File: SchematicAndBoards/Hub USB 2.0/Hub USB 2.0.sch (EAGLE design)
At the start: 29 parts, among them IC1 STM32F10XCXT6, IC2 MCP1703CB, IC3 IC_USBLC6-2, Q1 KX-7T 16.0 MHz, X1 USB-A

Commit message: Update schematic and boards
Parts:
- IC1: device stm32F:STM32F10XCXT6 -> stm32:STM32F10XCXT6
- IC3: value IC_USBLC6-2 -> USBLC6
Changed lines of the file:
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@@
 <?xml version="1.0" encoding="utf-8"?>
 <!DOCTYPE eagle SYSTEM "eagle.dtd">
-<eagle version="7.7.0">
+<eagle version="8.2.1">
 <drawing>
 <settings>
@@
 <layer number="56" name="wert" color="7" fill="1" visible="no" active="no"/>
 <layer number="57" name="tCAD" color="7" fill="1" visible="no" active="no"/>
+<layer number="59" name="tCarbon" color="7" fill="1" visible="no" active="no"/>
+<layer number="60" name="bCarbon" color="7" fill="1" visible="no" active="no"/>
 <layer number="90" name="Modules" color="5" fill="1" visible="yes" active="yes"/>
 <layer number="91" name="Nets" color="2" fill="1" visible="yes" active="yes"/>
@@
 <layer number="127" name="_tValues" color="7" fill="1" visible="no" active="yes"/>
 <layer number="128" name="_bValues" color="7" fill="1" visible="no" active="yes"/>
+<layer number="129" name="Mask" color="7" fill="1" visible="yes" active="yes"/>
 <layer number="131" name="tAdjust" color="7" fill="1" visible="no" active="yes"/>
 <layer number="132" name="bAdjust" color="7" fill="1" visible="no" active="yes"/>
@@
 <layer number="223" name="223bmp" color="24" fill="1" visible="no" active="no"/>
 <layer number="224" name="224bmp" color="25" fill="1" visible="no" active="no"/>
+<layer number="225" name="225bmp" color="7" fill="1" visible="yes" active="yes"/>
+<layer number="226" name="226bmp" color="7" fill="1" visible="yes" active="yes"/>
+<layer number="227" name="227bmp" color="7" fill="1" visible="yes" active="yes"/>
+<layer number="228" name="228bmp" color="7" fill="1" visible="yes" active="yes"/>
+<layer number="229" name="229bmp" color="7" fill="1" visible="yes" active="yes"/>
+<layer number="230" name="230bmp" color="7" fill="1" visible="yes" active="yes"/>
 <layer number="231" name="Eagle3D_PG1" color="7" fill="1" visible="no" active="no"/>
 <layer number="232" name="Eagle3D_PG2" color="7" fill="1" visible="no" active="no"/>
@@
 <layer number="251" name="SMDround" color="7" fill="1" visible="no" active="no"/>
 <layer number="254" name="cooling" color="7" fill="1" visible="no" active="yes"/>
+<layer number="255" name="routoute" color="7" fill="1" visible="yes" active="yes"/>
 </layers>
 <schematic xreflabel="%F%N/%S.%C%R" xrefpart="/%S.%C%R">
@@
 <parts>
 <part name="X1" library="adafruit" deviceset="USB-A" device=""/>
-<part name="IC1" library="stm32F" deviceset="STM32F10XCXT6" device=""/>
+<part name="IC1" library="stm32" deviceset="STM32F10XCXT6" device=""/>
 <part name="Q1" library="Eagle-JeeLabs" deviceset="CRYSTAL" device="3.2X2.5" value="KX-7T 16.0 MHz"/>
 <part name="R1" library="resistor" deviceset="R-EU_" device="R0805" value="22"/>
@@
 <part name="C11" library="resistor" deviceset="C-EU" device="C0805" value="0.01uF"/>
 <part name="C12" library="resistor" deviceset="C-EU" device="C0805" value="0.01uF"/>
-<part name="IC3" library="dp_devices" deviceset="IC_USBLC6-2" device=""/>
+<part name="IC3" library="dp_devices" deviceset="IC_USBLC6-2" device="" value="USBLC6"/>
 <part name="Q2" library="semicon-smd-ipc" deviceset="PNP-TRANSISTOR_" device="SOT23"/>
 <part name="U$2" library="RemoteSwitchComponents" deviceset="AS07-M1101S" device=""/>

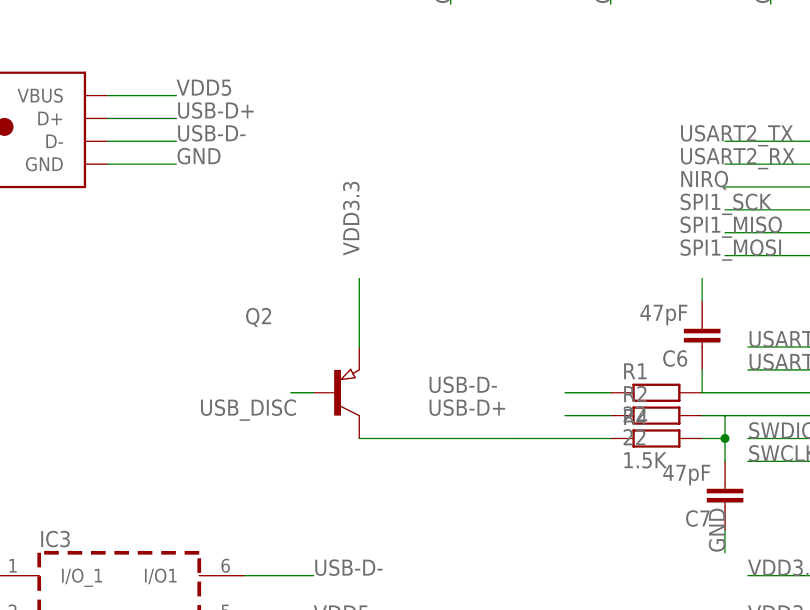
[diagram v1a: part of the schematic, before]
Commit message: Update Hub USB 2.0 schematic
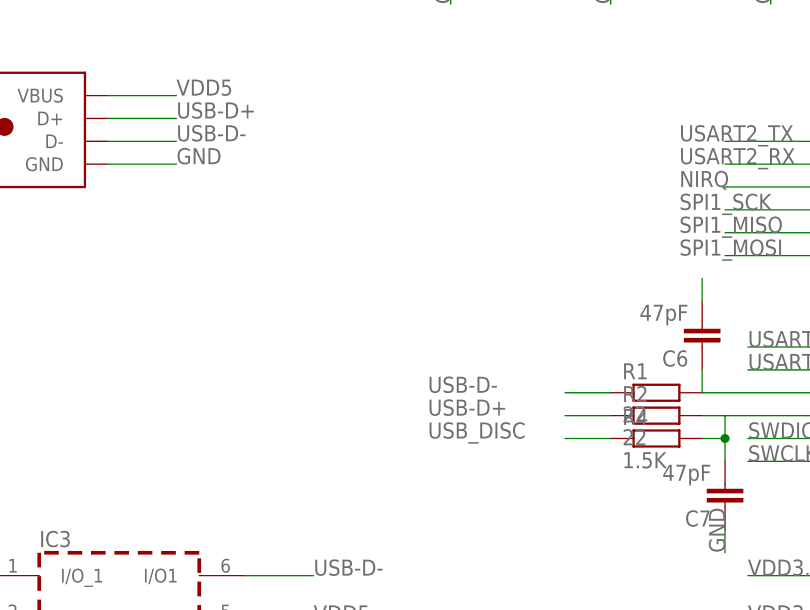
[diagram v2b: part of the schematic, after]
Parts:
- removed Q2: (no value), semicon-smd-ipc:PNP-TRANSISTOR_SOT23
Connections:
- removed net N$8: Q2.C, R4.1
- net USB_DISC: now also R4.1; no longer Q2.B
- net VDD3.3: no longer Q2.E
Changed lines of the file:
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@@
 <?xml version="1.0" encoding="utf-8"?>
 <!DOCTYPE eagle SYSTEM "eagle.dtd">
-<eagle version="8.2.1">
+<eagle version="7.7.0">
 <drawing>
 <settings>
@@
 <part name="C12" library="resistor" deviceset="C-EU" device="C0805" value="0.01uF"/>
 <part name="IC3" library="dp_devices" deviceset="IC_USBLC6-2" device="" value="USBLC6"/>
-<part name="Q2" library="semicon-smd-ipc" deviceset="PNP-TRANSISTOR_" device="SOT23"/>
 <part name="U$2" library="RemoteSwitchComponents" deviceset="AS07-M1101S" device=""/>
 </parts>
@@
 <instance part="C12" gate="G$1" x="114.3" y="109.22" rot="R180"/>
 <instance part="IC3" gate="G$1" x="2.54" y="22.86"/>
-<instance part="Q2" gate="G$1" x="17.78" y="55.88"/>
 <instance part="U$2" gate="G$1" x="182.88" y="-10.16"/>
 </instances>
@@
 </segment>
 <segment>
-<pinref part="Q2" gate="G$1" pin="E"/>
-<wire x1="20.32" y1="60.96" x2="20.32" y2="68.58" width="0.1524" layer="91"/>
-<label x="20.32" y="71.12" size="1.778" layer="95" rot="R90"/>
-</segment>
-<segment>
 <pinref part="U$2" gate="G$1" pin="VDD"/>
 <wire x1="170.18" y1="0" x2="157.48" y2="0" width="0.1524" layer="91"/>
@@
 </segment>
 </net>
-<net name="N$8" class="0">
-<segment>
-<pinref part="Q2" gate="G$1" pin="C"/>
-<wire x1="20.32" y1="50.8" x2="38.1" y2="50.8" width="0.1524" layer="91"/>
-</segment>
-<segment>
-<pinref part="R4" gate="G$1" pin="1"/>
-<wire x1="48.26" y1="50.8" x2="38.1" y2="50.8" width="0.1524" layer="91"/>
-</segment>
-</net>
 <net name="USB_DISC" class="0">
 <segment>
@@
 </segment>
 <segment>
-<pinref part="Q2" gate="G$1" pin="B"/>
-<wire x1="15.24" y1="55.88" x2="12.7" y2="55.88" width="0.1524" layer="91"/>
-<label x="2.54" y="53.34" size="1.778" layer="95"/>
-</segment>
-</net>
+<pinref part="R4" gate="G$1" pin="1"/>
+<wire x1="48.26" y1="50.8" x2="43.18" y2="50.8" width="0.1524" layer="91"/>
+<label x="27.94" y="50.8" size="1.778" layer="95"/>
+</segment>
+</net>

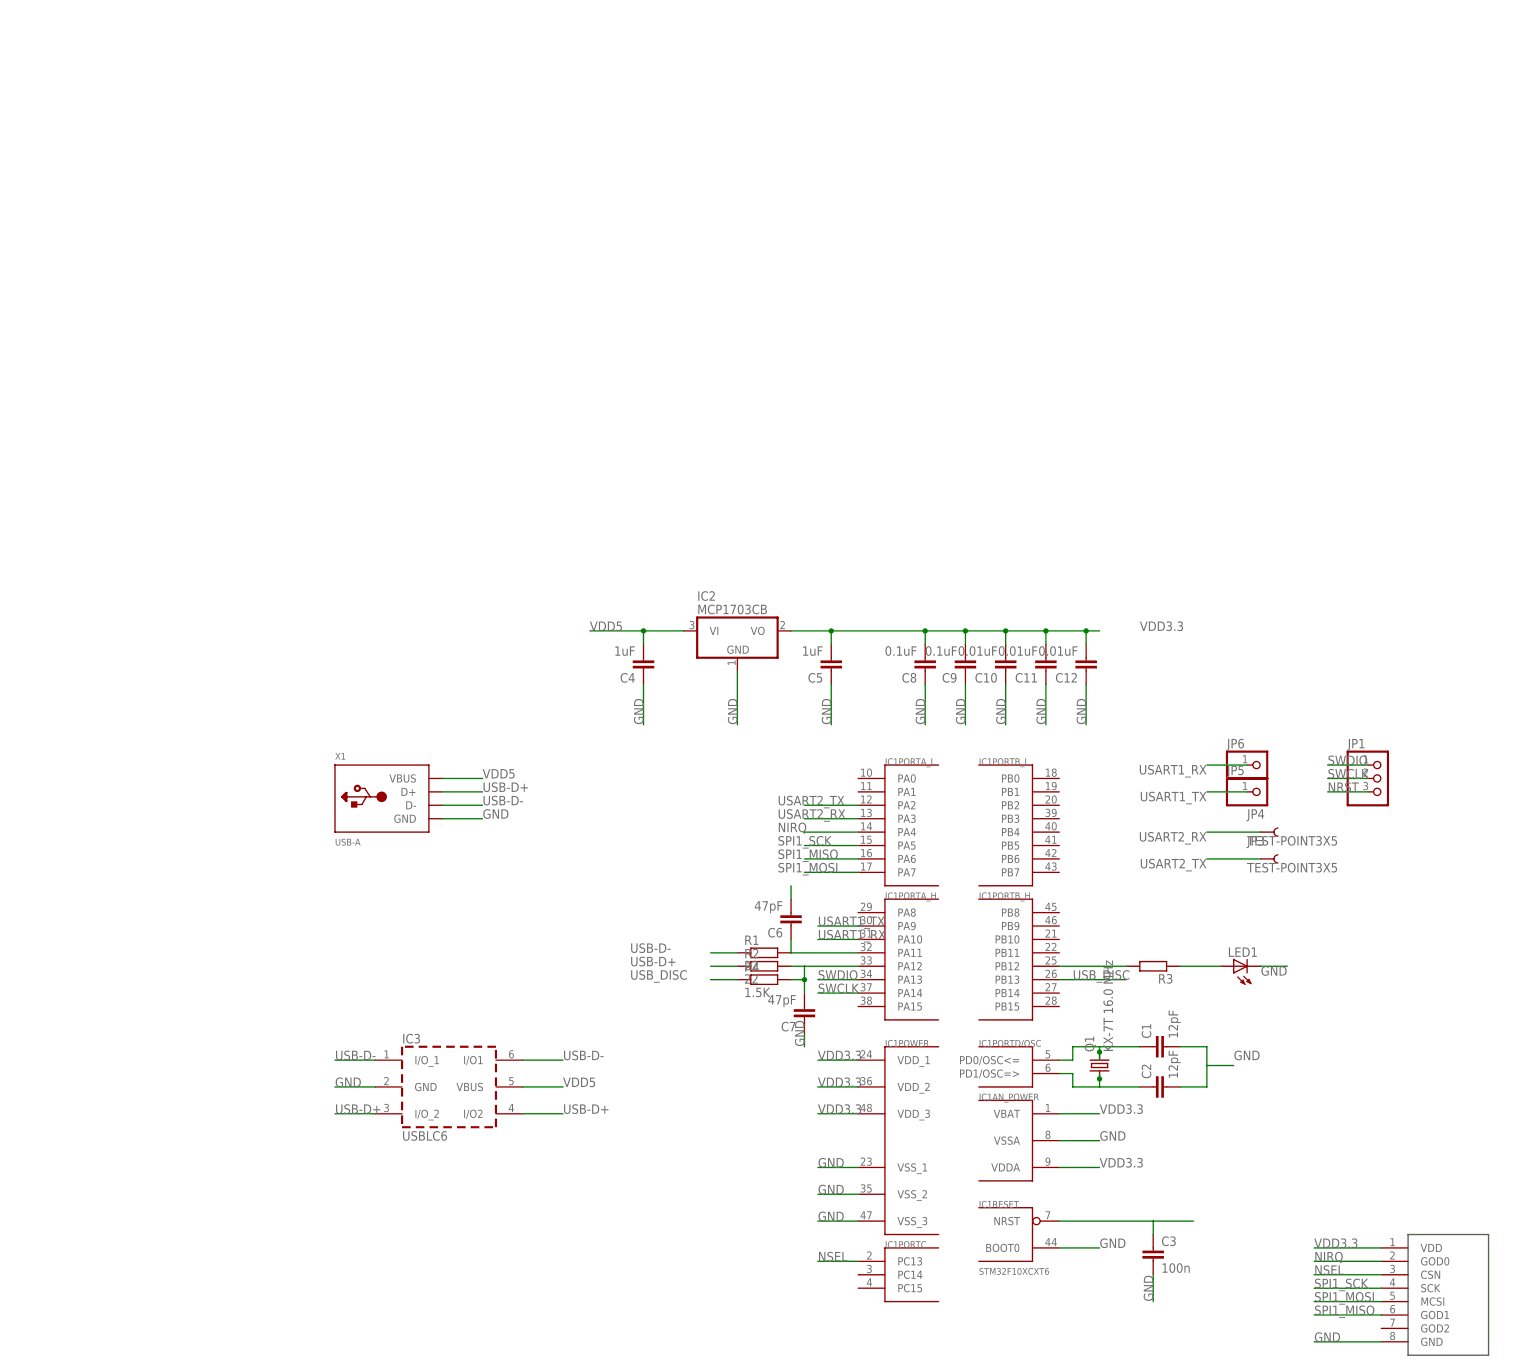
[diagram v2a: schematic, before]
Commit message: Update Hub USB 2.0, add achematic in PDF
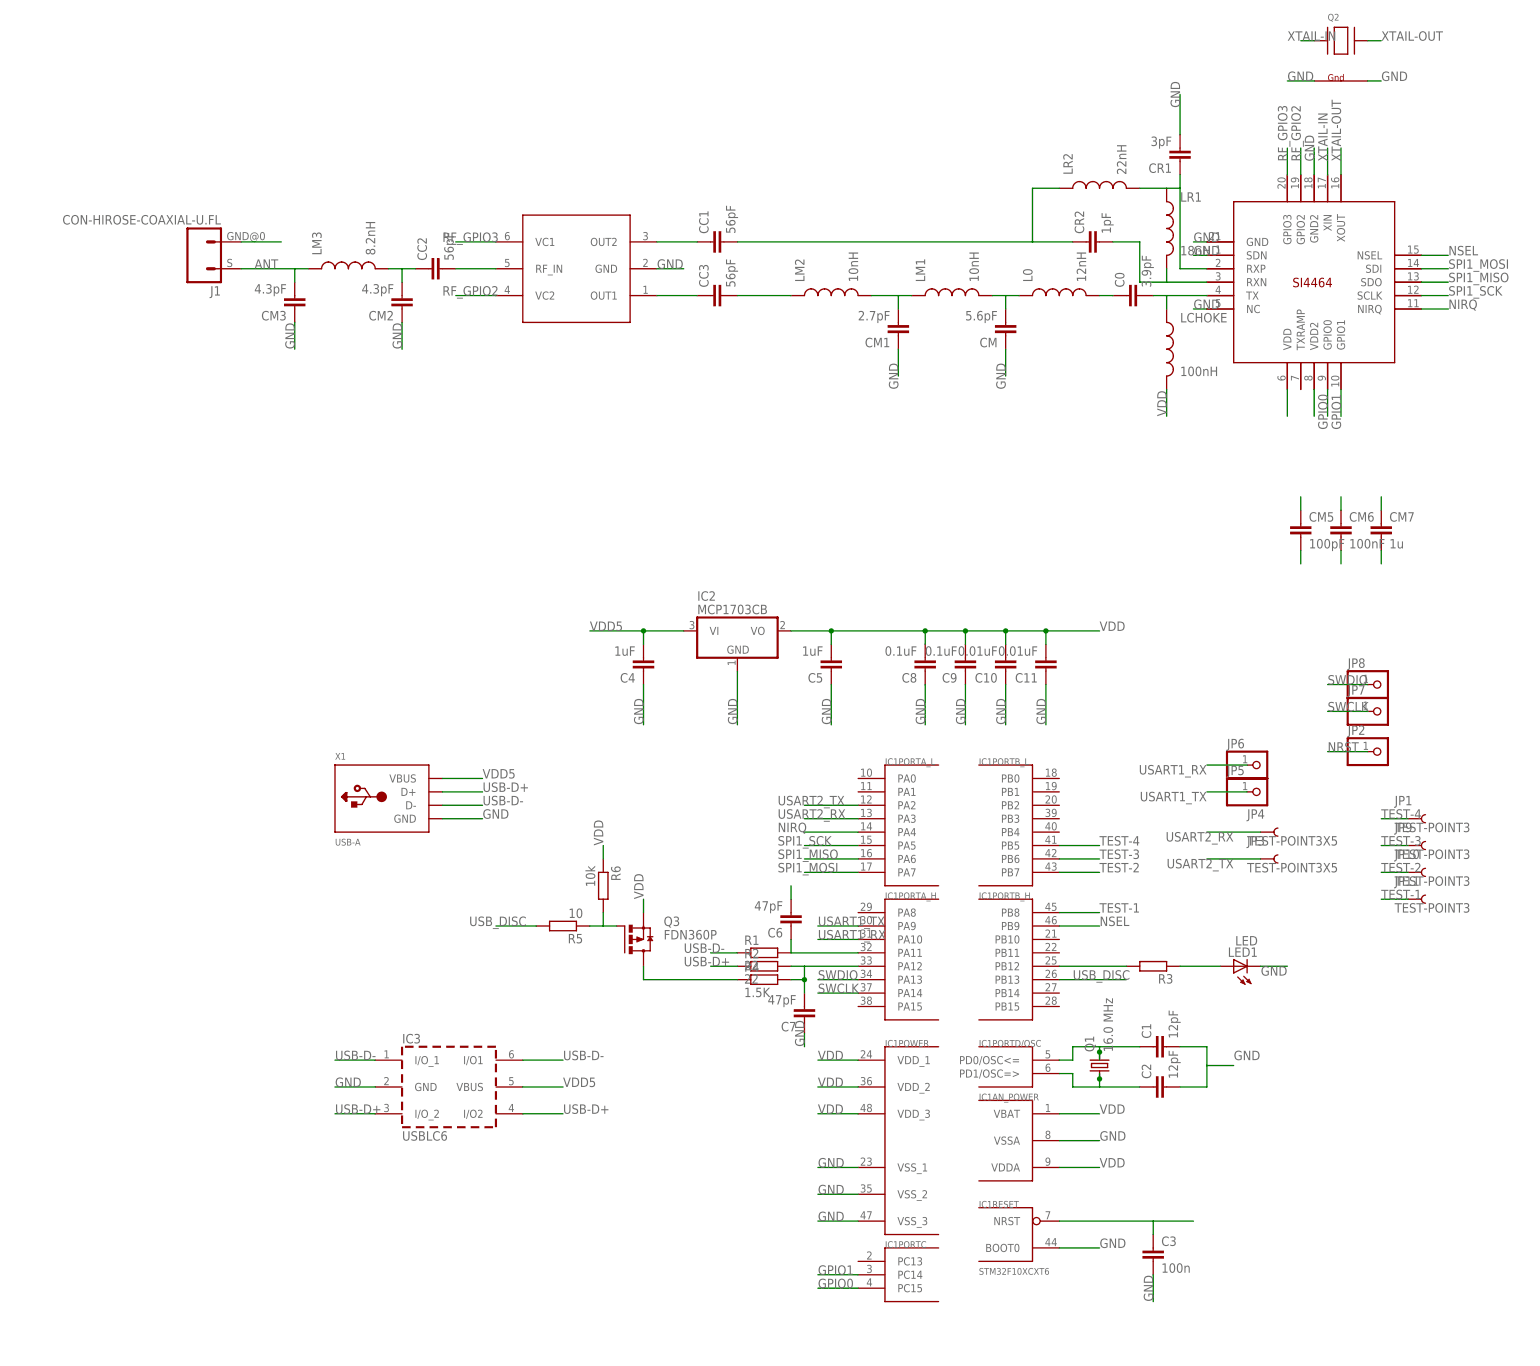
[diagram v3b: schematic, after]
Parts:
- removed C12: 0.01uF, resistor:C-EUC0805
- added C0: 3.9pF, resistor:C-EUC0402
- added CC1, CC2, CC3: 56pF, resistor:C-EUC0402
- added CM: 5.6pF, resistor:C-EUC0402
- added CM1: 2.7pF, resistor:C-EUC0402
- added CM2, CM3: 4.3pF, resistor:C-EUC0402
- added CM5: 100pF, resistor:C-EUC0402
- added CM6: 100nF, resistor:C-EUC0402
- added CM7: 1u, resistor:C-EUC0402
- added CR1: 3pF, resistor:C-EUC0402
- added CR2: 1pF, resistor:C-EUC0402
- added J1: CON-HIROSE-COAXIAL-U.FL, m-pad-2.1:CON-HIROSE-COAXIAL-U.FL
- added JP10, JP11, JP9: TEST-POINT3, SparkFun-Passives:TEST-POINT3
- added JP2, JP7, JP8: (no value), pinhead:PINHD-1X1
- added L0: 12nH, SparkFun-Passives:INDUCTOR0402
- added LCHOKE: 100nH, SparkFun-Passives:INDUCTOR0402
- added LM1, LM2: 10nH, SparkFun-Passives:INDUCTOR0402
- added LM3: 8.2nH, SparkFun-Passives:INDUCTOR0402
- added LR1: 18nH, SparkFun-Passives:INDUCTOR0402
- added LR2: 22nH, SparkFun-Passives:INDUCTOR0402
- added Q2: (no value), adafruit:XTAL-4-3225
- added Q3: FDN360P, transistor-power:FDN360P
- added R5: 10, resistor:R-EU_R0805
- added R6: 10k, resistor:R-EU_R0805
- added U$1: SI4464, Ava:SI4464
- JP1: value (none) -> TEST-POINT3; device adafruit:PINHD-1X3 -> SparkFun-Passives:TEST-POINT3
- LED1: value (none) -> LED
- Q1: value KX-7T 16.0 MHz -> 16.0 MHz
- U$2: value AS07-M1101S -> UPG2179TB; device RemoteSwitchComponents:AS07-M1101S -> Ava:UPG2179TB
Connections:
- removed net VDD3.3: C10.2, C11.2, C12.2, C5.2, C8.2, C9.2, IC1AN_POWER.VBAT, IC1AN_POWER.VDDA, IC1POWER.VDD_1, IC1POWER.VDD_2, IC1POWER.VDD_3, IC2.VO, U$2.VDD
- new net ANT: CM3.2, J1.1, LM3.1
- new net GPIO0: IC1PORTC.PC15, U$1.GPIO0
- new net GPIO1: IC1PORTC.PC14, U$1.GPIO1
- new net N$11: CC3.1, U$2.OUT1
- new net N$12: CR2.2, LR1.2, U$1.RXN
- new net N$13: CC1.1, U$2.OUT2
- new net N$14: CR1.1, LR1.1, LR2.2, U$1.RXP
- new net N$16: CC2.2, U$2.RF_IN
- new net N$17: CC3.2, LM2.1
- new net N$18: CC1.2, CR2.1, LR2.1
- new net N$19: Q3.D, R4.1
- new net N$20: Q3.G, R5.1, R6.2
- new net N$3: C0.2, LCHOKE.1, U$1.TX
- new net N$5: C0.1, L0.2
- new net N$7: CM.2, L0.1, LM1.2
- new net N$8: CM1.2, LM1.1, LM2.2
- new net N$9: CC2.1, CM2.2, LM3.2
- new net RF_GPIO2: U$1.GPIO2, U$2.VC2
- new net RF_GPIO3: U$1.GPIO3, U$2.VC1
- new net TEST-1: IC1PORTB_H.PB8, JP11.1
- new net TEST-2: IC1PORTB_L.PB7, JP10.1
- new net TEST-3: IC1PORTB_L.PB6, JP9.1
- new net TEST-4: IC1PORTB_L.PB5, JP1.1
- new net VDD: C10.2, C11.2, C5.2, C8.2, C9.2, CM5.1, CM6.1, CM7.1, IC1AN_POWER.VBAT, IC1AN_POWER.VDDA, IC1POWER.VDD_1, IC1POWER.VDD_2, IC1POWER.VDD_3, IC2.VO, LCHOKE.2, Q3.S, R6.1, U$1.VDD, U$1.VDD2
- new net XTAIL-IN: Q2.X1, U$1.XIN
- new net XTAIL-OUT: Q2.X2, U$1.XOUT
- net GND: now also CM.1, CM1.1, CM2.1, CM3.1, CM5.2, CM6.2, CM7.2, CR1.2, J1.2, Q2.G1, Q2.G2, U$1.GND, U$1.GND2, U$1.NC , U$1.SDN; no longer C12.1
- net NIRQ: now also U$1.NIRQ; no longer U$2.GOD0
- net NRST: now also JP2.1; no longer JP1.3
- net NSEL: now also IC1PORTB_H.PB9, U$1.NSEL; no longer IC1PORTC.PC13, U$2.CSN
- net SPI1_MISO: now also U$1.SDO; no longer U$2.GOD1
- net SPI1_MOSI: now also U$1.SDI; no longer U$2.MCSI
- net SPI1_SCK: now also U$1.SCLK; no longer U$2.SCK
- net SWCLK: now also JP7.1; no longer JP1.2
- net SWDIO: now also JP8.1; no longer JP1.1
- net USB_DISC: now also R5.2; no longer R4.1
